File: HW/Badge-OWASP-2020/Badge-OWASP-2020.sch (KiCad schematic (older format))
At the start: 7 parts

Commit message: Add MMBT3904
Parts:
- added Q? (x2): MMBT3904, Package_TO_SOT_SMD:SOT-23, symbol Transistor_BJT:MMBT3904
- added R? (x2): R, symbol Device:R
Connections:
- net DTR: now also Q?.3 (C), R?.2
- new net: Q?.1 (B), R?.1 (x2)
- new net GPIO0: Q?.2 (E)
- new net RST: Q?.2 (E), Q?.3 (C), R?.2
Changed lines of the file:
@@
 Wire Wire Line
 	1100 7300 1500 7300
+$Comp
+L Transistor_BJT:MMBT3904 Q?
+U 1 1 5DF429DE
+P 5850 6200
+F 0 "Q?" H 6041 6246 50  0000 L CNN
+F 1 "MMBT3904" H 6041 6155 50  0000 L CNN
+F 2 "Package_TO_SOT_SMD:SOT-23" H 6050 6125 50  0001 L CIN
+F 3 "https://www.fairchildsemi.com/datasheets/2N/2N3904.pdf" H 5850 6200 50  0001 L CNN
+	1    5850 6200
+	1    0    0    -1
+$EndComp
+$Comp
+L Transistor_BJT:MMBT3904 Q?
+U 1 1 5DF42F4A
+P 5850 6800
+F 0 "Q?" H 6041 6846 50  0000 L CNN
+F 1 "MMBT3904" H 6041 6755 50  0000 L CNN
+F 2 "Package_TO_SOT_SMD:SOT-23" H 6050 6725 50  0001 L CIN
+F 3 "https://www.fairchildsemi.com/datasheets/2N/2N3904.pdf" H 5850 6800 50  0001 L CNN
+	1    5850 6800
+	1    0    0    -1
+$EndComp
+$Comp
+L Device:R R?
+U 1 1 5DF43EDC
+P 5250 6200
+F 0 "R?" V 5043 6200 50  0000 C CNN
+F 1 "R" V 5134 6200 50  0000 C CNN
+F 2 "" V 5180 6200 50  0001 C CNN
+F 3 "~" H 5250 6200 50  0001 C CNN
+	1    5250 6200
+	0    1    1    0
+$EndComp
+$Comp
+L Device:R R?
+U 1 1 5DF44157
+P 5250 6800
+F 0 "R?" V 5043 6800 50  0000 C CNN
+F 1 "R" V 5134 6800 50  0000 C CNN
+F 2 "" V 5180 6800 50  0001 C CNN
+F 3 "~" H 5250 6800 50  0001 C CNN
+	1    5250 6800
+	0    1    1    0
+$EndComp
+Wire Wire Line
+	5650 6200 5400 6200
+Wire Wire Line
+	5650 6800 5400 6800
+Text Label 4800 5900 0    50   ~ 0
+RST
+Text Label 4800 6800 0    50   ~ 0
+RST
+Wire Wire Line
+	5100 6800 5000 6800
+Wire Wire Line
+	5950 6000 5950 5900
+Wire Wire Line
+	5950 5900 4800 5900
+Text Label 4800 6200 0    50   ~ 0
+DTR
+Wire Wire Line
+	5100 6200 5050 6200
+Text Label 4800 7050 0    50   ~ 0
+GPIO0
+Wire Wire Line
+	5950 7000 5950 7050
+Wire Wire Line
+	5950 7050 4800 7050
+Wire Wire Line
+	5950 6600 5950 6550
+Wire Wire Line
+	5950 6550 5050 6550
+Wire Wire Line
+	5050 6550 5050 6200
+Connection ~ 5050 6200
+Wire Wire Line
+	5050 6200 4800 6200
+Wire Wire Line
+	5950 6400 5000 6400
+Wire Wire Line
+	5000 6400 5000 6800
+Connection ~ 5000 6800
+Wire Wire Line
+	5000 6800 4800 6800
 $EndSCHEMATC

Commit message: Change RTS
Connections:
- net RTS: now also Q?.2 (E), R?.2
- removed net RST: Q?.2 (E), Q?.3 (C), R?.2
- new net EN: Q?.3 (C)
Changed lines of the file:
@@
 	5650 6800 5400 6800
 Text Label 4800 5900 0    50   ~ 0
-RST
+EN
 Text Label 4800 6800 0    50   ~ 0
-RST
+RTS
 Wire Wire Line
 	5100 6800 5000 6800

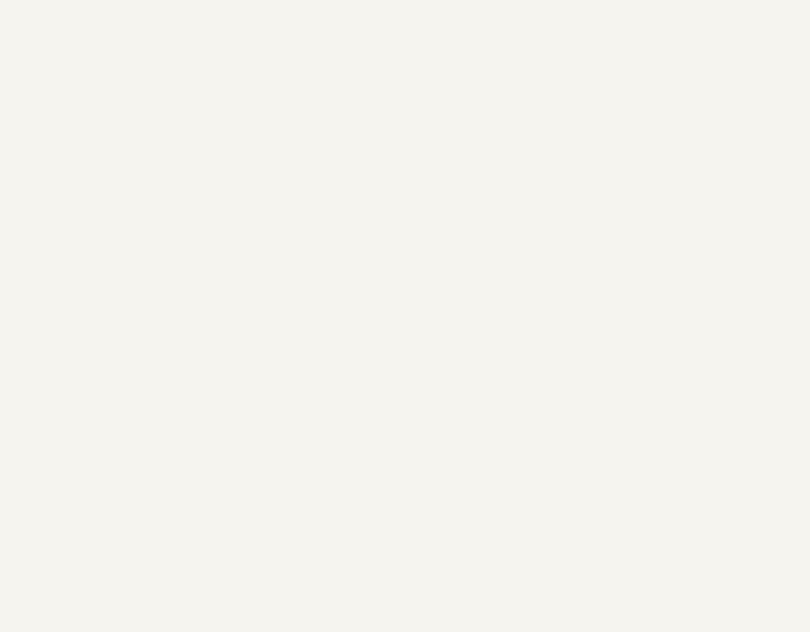
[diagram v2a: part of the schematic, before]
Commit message: C and GND WS2812B
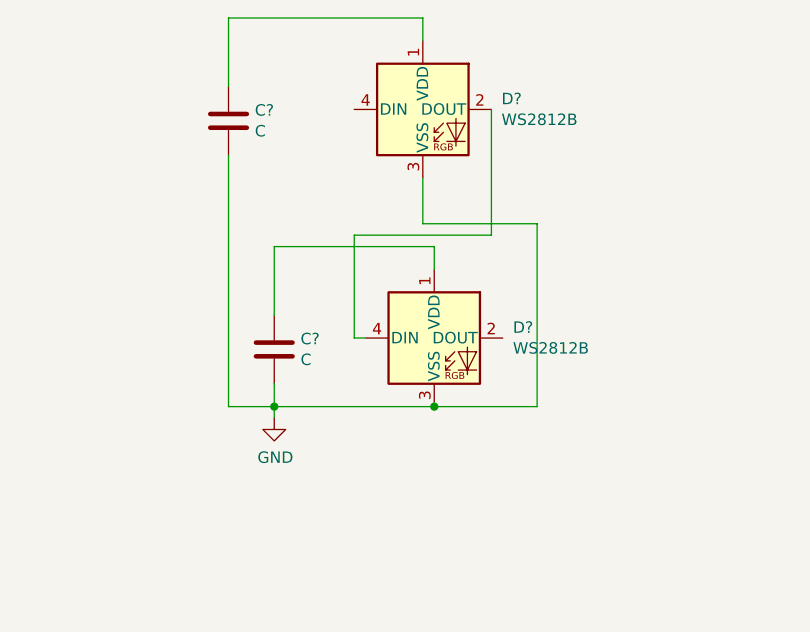
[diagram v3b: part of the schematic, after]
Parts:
- added C? (x2): C, symbol Device:C
- added D? (x2): WS2812B, LED_SMD:LED_WS2812B_PLCC4_5.0x5.0mm_P3.2mm, symbol LED:WS2812B
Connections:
- net GND: now also C?.2, C?.2, D?.3 (VSS), D?.3 (VSS)
- new net: C?.1, D?.1 (VDD) (x2)
- new net: D?.2 (DOUT), D?.4 (DIN)
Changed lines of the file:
@@
 Wire Wire Line
 	5000 6800 4800 6800
+$Comp
+L LED:WS2812B D?
+U 1 1 5DF4AD3B
+P 6000 1700
+F 0 "D?" H 6344 1746 50  0000 L CNN
+F 1 "WS2812B" H 6344 1655 50  0000 L CNN
+F 2 "LED_SMD:LED_WS2812B_PLCC4_5.0x5.0mm_P3.2mm" H 6050 1400 50  0001 L TNN
+F 3 "https://cdn-shop.adafruit.com/datasheets/WS2812B.pdf" H 6100 1325 50  0001 L TNN
+	1    6000 1700
+	1    0    0    -1
+$EndComp
+$Comp
+L LED:WS2812B D?
+U 1 1 5DF4C388
+P 6050 2700
+F 0 "D?" H 6394 2746 50  0000 L CNN
+F 1 "WS2812B" H 6394 2655 50  0000 L CNN
+F 2 "LED_SMD:LED_WS2812B_PLCC4_5.0x5.0mm_P3.2mm" H 6100 2400 50  0001 L TNN
+F 3 "https://cdn-shop.adafruit.com/datasheets/WS2812B.pdf" H 6150 2325 50  0001 L TNN
+	1    6050 2700
+	1    0    0    -1
+$EndComp
+$Comp
+L Device:C C?
+U 1 1 5DF4D0A0
+P 5150 1750
+F 0 "C?" H 5265 1796 50  0000 L CNN
+F 1 "C" H 5265 1705 50  0000 L CNN
+F 2 "" H 5188 1600 50  0001 C CNN
+F 3 "~" H 5150 1750 50  0001 C CNN
+	1    5150 1750
+	1    0    0    -1
+$EndComp
+$Comp
+L Device:C C?
+U 1 1 5DF4D5CB
+P 5350 2750
+F 0 "C?" H 5465 2796 50  0000 L CNN
+F 1 "C" H 5465 2705 50  0000 L CNN
+F 2 "" H 5388 2600 50  0001 C CNN
+F 3 "~" H 5350 2750 50  0001 C CNN
+	1    5350 2750
+	1    0    0    -1
+$EndComp
+Wire Wire Line
+	6000 1400 6000 1300
+Wire Wire Line
+	6000 1300 5150 1300
+Wire Wire Line
+	5150 1300 5150 1600
+Wire Wire Line
+	6050 2400 6050 2300
+Wire Wire Line
+	6050 2300 5350 2300
+Wire Wire Line
+	5350 2300 5350 2600
+Wire Wire Line
+	5350 2900 5350 3000
+Wire Wire Line
+	5150 3000 5350 3000
+Wire Wire Line
+	5150 1900 5150 3000
+Connection ~ 5350 3000
+Wire Wire Line
+	5350 3000 5350 3050
+$Comp
+L power:GND #PWR?
+U 1 1 5DF54417
+P 5350 3050
+F 0 "#PWR?" H 5350 2800 50  0001 C CNN
+F 1 "GND" H 5355 2877 50  0000 C CNN
+F 2 "" H 5350 3050 50  0001 C CNN
+F 3 "" H 5350 3050 50  0001 C CNN
+	1    5350 3050
+	1    0    0    -1
+$EndComp
+Wire Wire Line
+	6300 1700 6300 2250
+Wire Wire Line
+	6300 2250 5700 2250
+Wire Wire Line
+	5700 2250 5700 2700
+Wire Wire Line
+	5700 2700 5750 2700
+Wire Wire Line
+	6000 2000 6000 2200
+Wire Wire Line
+	6000 2200 6500 2200
+Wire Wire Line
+	6500 2200 6500 3000
+Wire Wire Line
+	5350 3000 6050 3000
+Connection ~ 6050 3000
+Wire Wire Line
+	6050 3000 6500 3000
 $EndSCHEMATC

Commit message: Values C and R
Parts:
- C? (x2): value C -> 4.7uF
- C? (x2): value C -> 0.1uF
- R? (x2): value R -> 10K
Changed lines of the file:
@@
 P 1950 7100
 F 0 "C?" H 2065 7146 50  0000 L CNN
-F 1 "C" H 2065 7055 50  0000 L CNN
+F 1 "4.7uF" H 2065 7055 50  0000 L CNN
 F 2 "" H 1988 6950 50  0001 C CNN
 F 3 "~" H 1950 7100 50  0001 C CNN
@@
 P 1100 7150
 F 0 "C?" H 1215 7196 50  0000 L CNN
-F 1 "C" H 1215 7105 50  0000 L CNN
+F 1 "4.7uF" H 1215 7105 50  0000 L CNN
 F 2 "" H 1138 7000 50  0001 C CNN
 F 3 "~" H 1100 7150 50  0001 C CNN
@@
 P 5250 6200
 F 0 "R?" V 5043 6200 50  0000 C CNN
-F 1 "R" V 5134 6200 50  0000 C CNN
+F 1 "10K" V 5134 6200 50  0000 C CNN
 F 2 "" V 5180 6200 50  0001 C CNN
 F 3 "~" H 5250 6200 50  0001 C CNN
@@
 P 5250 6800
 F 0 "R?" V 5043 6800 50  0000 C CNN
-F 1 "R" V 5134 6800 50  0000 C CNN
+F 1 "10K" V 5134 6800 50  0000 C CNN
 F 2 "" V 5180 6800 50  0001 C CNN
 F 3 "~" H 5250 6800 50  0001 C CNN
@@
 P 5150 1750
 F 0 "C?" H 5265 1796 50  0000 L CNN
-F 1 "C" H 5265 1705 50  0000 L CNN
+F 1 "0.1uF" H 5265 1705 50  0000 L CNN
 F 2 "" H 5188 1600 50  0001 C CNN
 F 3 "~" H 5150 1750 50  0001 C CNN
@@
 P 5350 2750
 F 0 "C?" H 5465 2796 50  0000 L CNN
-F 1 "C" H 5465 2705 50  0000 L CNN
+F 1 "0.1uF" H 5465 2705 50  0000 L CNN
 F 2 "" H 5388 2600 50  0001 C CNN
 F 3 "~" H 5350 2750 50  0001 C CNN

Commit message: Screen OLED
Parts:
- added J?: Screw_Terminal_01x04, symbol Connector:Screw_Terminal_01x04
- added R? (x2): 10K, symbol Device:R
- D?: value D -> MBR120
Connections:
- net +3V3: now also J?.2 (Pin_2), R?.2, R?.2
- net GND: now also J?.1 (Pin_1)
- new net SCL: J?.3 (Pin_3), R?.1
- new net SDA: J?.4 (Pin_4), R?.1
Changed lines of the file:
@@
 P 900 6800
 F 0 "D?" H 900 6584 50  0000 C CNN
-F 1 "D" H 900 6675 50  0000 C CNN
+F 1 "MBR120" H 900 6675 50  0000 C CNN
 F 2 "" H 900 6800 50  0001 C CNN
 F 3 "~" H 900 6800 50  0001 C CNN
@@
 Wire Wire Line
 	6050 3000 6500 3000
+$Comp
+L Connector:Screw_Terminal_01x04 J?
+U 1 1 5DF60FAB
+P 3900 3800
+F 0 "J?" H 3980 3792 50  0000 L CNN
+F 1 "Screw_Terminal_01x04" H 3980 3701 50  0000 L CNN
+F 2 "" H 3900 3800 50  0001 C CNN
+F 3 "~" H 3900 3800 50  0001 C CNN
+	1    3900 3800
+	1    0    0    -1
+$EndComp
+$Comp
+L Device:R R?
+U 1 1 5DF5B194
+P 2950 3700
+F 0 "R?" V 2743 3700 50  0000 C CNN
+F 1 "10K" V 2834 3700 50  0000 C CNN
+F 2 "" V 2880 3700 50  0001 C CNN
+F 3 "~" H 2950 3700 50  0001 C CNN
+	1    2950 3700
+	-1   0    0    1
+$EndComp
+Wire Wire Line
+	2950 3500 3150 3500
+$Comp
+L Device:R R?
+U 1 1 5DF5B633
+P 3350 3650
+F 0 "R?" V 3143 3650 50  0000 C CNN
+F 1 "10K" V 3234 3650 50  0000 C CNN
+F 2 "" V 3280 3650 50  0001 C CNN
+F 3 "~" H 3350 3650 50  0001 C CNN
+	1    3350 3650
+	-1   0    0    1
+$EndComp
+Wire Wire Line
+	3700 3800 3500 3800
+Wire Wire Line
+	3500 3800 3500 3350
+Wire Wire Line
+	3500 3350 3150 3350
+Wire Wire Line
+	3150 3350 3150 3500
+Connection ~ 3150 3500
+Wire Wire Line
+	3150 3500 3350 3500
+$Comp
+L power:+3.3V #PWR?
+U 1 1 5DF7108A
+P 3150 3350
+F 0 "#PWR?" H 3150 3200 50  0001 C CNN
+F 1 "+3.3V" H 3165 3523 50  0000 C CNN
+F 2 "" H 3150 3350 50  0001 C CNN
+F 3 "" H 3150 3350 50  0001 C CNN
+	1    3150 3350
+	1    0    0    -1
+$EndComp
+Connection ~ 3150 3350
+Text Label 2750 4000 0    50   ~ 0
+SDA
+Text Label 2750 3900 0    50   ~ 0
+SCL
+Wire Wire Line
+	3700 4000 3350 4000
+Wire Wire Line
+	3350 3800 3350 4000
+Connection ~ 3350 4000
+Wire Wire Line
+	3350 4000 2750 4000
+Wire Wire Line
+	2950 3500 2950 3550
+Wire Wire Line
+	2750 3900 2950 3900
+Wire Wire Line
+	2950 3850 2950 3900
+Connection ~ 2950 3900
+Wire Wire Line
+	2950 3900 3700 3900
+Wire Wire Line
+	3700 3700 3550 3700
+Wire Wire Line
+	3550 3700 3550 4200
+$Comp
+L power:GND #PWR?
+U 1 1 5DF7CD80
+P 3550 4200
+F 0 "#PWR?" H 3550 3950 50  0001 C CNN
+F 1 "GND" H 3555 4027 50  0000 C CNN
+F 2 "" H 3550 4200 50  0001 C CNN
+F 3 "" H 3550 4200 50  0001 C CNN
+	1    3550 4200
+	1    0    0    -1
+$EndComp
 $EndSCHEMATC

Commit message: ESP32
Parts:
- added C?: 0.1uF, symbol Device:C
- added J?: Conn_02x03_Odd_Even, symbol Connector_Generic:Conn_02x03_Odd_Even
- added R?: R, symbol Device:R
- added SW?: RST, symbol Switch:SW_Push
- added SW?: BOOT, symbol Switch:SW_Push
- added U?: ESP32-WROOM-32, RF_Module:ESP32-WROOM-32, symbol RF_Module:ESP32-WROOM-32
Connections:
- net +3V3: now also C?.1, C?.1, D?.1 (VDD), D?.1 (VDD), C?.1, J?.2 (Pin_2), U?.2 (VDD)
- net EN: now also SW?.2, U?.3 (EN)
- net GND: now also C?.2, J?.1 (Pin_1), SW?.1, SW?.1, U?.1 (GND), U?.15 (GND), U?.38 (GND)
- net GPIO0: now also SW?.2, U?.25 (IO0)
- net SCL: now also J?.3 (Pin_3), U?.36 (IO22)
- net SDA: now also J?.4 (Pin_4), U?.33 (IO21)
- net D+: now reaches J?.3 (D+), U?.5 (UD+)
- net D-: now reaches J?.2 (D-), U?.6 (UD-)
- net np: now reaches D?.4 (DIN)
- net np: now also R?.1
- new net: R?.2, U?.23 (IO15)
- new net GPIO1: J?.6 (Pin_6), U?.24 (IO2)
- new net GPIO2: J?.5 (Pin_5), U?.26 (IO4)
- new net RX: U?.35 (TXD0/IO1)
- new net TX: U?.34 (RXD0/IO3)
- no-connect marks 4 -> 29
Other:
- moved on the sheet: C?, D?, F?, J?, Q?, R?, U?

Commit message: footprints
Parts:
- C1, C2, C3, C4, C5: renamed from C?; footprint (none) -> Capacitor_SMD:C_0805_2012Metric_Pad1.15x1.40mm_HandSolder
- D1: renamed from D?; footprint (none) -> Diode_SMD:D_SOD-123F
- F1: renamed from F?; footprint (none) -> Fuse:Fuse_1812_4532Metric_Pad1.30x3.40mm_HandSolder
- J1: renamed from J?; footprint (none) -> Connector_PinHeader_2.54mm:PinHeader_1x04_P2.54mm_Vertical
- J2: renamed from J?; footprint (none) -> Connector_USB:USB_Micro-B_Wuerth_629105150521
- J3: renamed from J?; footprint (none) -> Connector_PinHeader_2.54mm:PinHeader_2x03_P2.54mm_Vertical
- R1, R2, R3, R4, R5: renamed from R?; footprint (none) -> Resistor_SMD:R_0805_2012Metric_Pad1.15x1.40mm_HandSolder
- SW1, SW2: renamed from SW?; footprint (none) -> Button_Switch_SMD:SW_SPST_TL3342
- gave numbers to parts that had none: 7

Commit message: Change footprints and add R
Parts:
- added R1: 10K, Resistor_SMD:R_0805_2012Metric_Pad1.15x1.40mm_HandSolder, symbol Device:R
- D2, D3: footprint LED_SMD:LED_WS2812B_PLCC4_5.0x5.0mm_P3.2mm -> LED_SMD:LED_SK6812MINI_PLCC4_3.5x3.5mm_P1.75mm
- R5: value R -> 470
- U3: symbol Interface_USB2:CH340C -> Badge-OWASP-2020-rescue:CH340C-Interface_USB2
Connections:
- net EN: now also R1.1; no longer SW1.2
- net VCC: now also R1.2
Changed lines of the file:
@@
 $EndDescr
 $Comp
-L Interface_USB2:CH340C U3
+L Badge-OWASP-2020-rescue:CH340C-Interface_USB2 U3
 U 1 1 5DF1A7B6
 P 9850 5550
@@
 F 0 "D2" H 1550 2300 50  0000 L CNN
 F 1 "WS2812B" H 1600 2400 50  0000 L CNN
-F 2 "LED_SMD:LED_WS2812B_PLCC4_5.0x5.0mm_P3.2mm" H 1450 1700 50  0001 L TNN
+F 2 "LED_SMD:LED_SK6812MINI_PLCC4_3.5x3.5mm_P1.75mm" H 1450 1700 50  0001 L TNN
 F 3 "https://cdn-shop.adafruit.com/datasheets/WS2812B.pdf" H 1500 1625 50  0001 L TNN
 	1    1400 2000
@@
 F 0 "D3" H 2600 2500 50  0000 L CNN
 F 1 "WS2812B" H 2600 2300 50  0000 L CNN
-F 2 "LED_SMD:LED_WS2812B_PLCC4_5.0x5.0mm_P3.2mm" H 2500 1700 50  0001 L TNN
+F 2 "LED_SMD:LED_SK6812MINI_PLCC4_3.5x3.5mm_P1.75mm" H 2500 1700 50  0001 L TNN
 F 3 "https://cdn-shop.adafruit.com/datasheets/WS2812B.pdf" H 2550 1625 50  0001 L TNN
 	1    2450 2000
@@
 Wire Wire Line
 	6950 1400 7150 1400
-Text Label 5600 1100 0    50   ~ 0
-EN
-Wire Wire Line
-	5750 1100 5600 1100
 NoConn ~ 5750 1300
 NoConn ~ 5750 1400
@@
 P 7400 2000
 F 0 "R5" V 7150 2050 50  0000 R CNN
-F 1 "R" V 7250 2000 50  0000 R CNN
+F 1 "470" V 7250 2000 50  0000 R CNN
 F 2 "Resistor_SMD:R_0805_2012Metric_Pad1.15x1.40mm_HandSolder" V 7330 2000 50  0001 C CNN
 F 3 "~" H 7400 2000 50  0001 C CNN
@@
 	1    0    0    -1
 $EndComp
-Text Label 5200 1700 0    50   ~ 0
+Text Label 5550 1100 0    50   ~ 0
 EN
 Text Label 5150 3050 0    50   ~ 0
@@
 Wire Wire Line
 	4600 1700 4600 1900
+Wire Wire Line
+	5350 1100 5750 1100
+$Comp
+L power:VCC #PWR026
+U 1 1 5DFD0640
+P 5350 700
+F 0 "#PWR026" H 5350 550 50  0001 C CNN
+F 1 "VCC" H 5367 873 50  0000 C CNN
+F 2 "" H 5350 700 50  0001 C CNN
+F 3 "" H 5350 700 50  0001 C CNN
+	1    5350 700
+	1    0    0    -1
+$EndComp
+$Comp
+L Device:R R1
+U 1 1 5DFC7D12
+P 5350 950
+F 0 "R1" V 5100 1000 50  0000 R CNN
+F 1 "10K" V 5200 950 50  0000 R CNN
+F 2 "Resistor_SMD:R_0805_2012Metric_Pad1.15x1.40mm_HandSolder" V 5280 950 50  0001 C CNN
+F 3 "~" H 5350 950 50  0001 C CNN
+	1    5350 950
+	-1   0    0    1
+$EndComp
+Wire Wire Line
+	5350 800  5350 700
 $EndSCHEMATC
